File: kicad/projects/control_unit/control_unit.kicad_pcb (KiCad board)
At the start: 2 copper layers, 177.8 x 76.2 mm, 20 parts, among them J1 Conn_01x11_Male, J2 Conn_01x04_Female, J3 Conn_01x08_Female, J4 Conn_01x34_Male, J5 Conn_01x16_Female, J6 Conn_01x16_Female, J7 Conn_01x08_Female, J8 Conn_01x01_Female, U1 28C256, U2 28C256, U3 28C256, U4 28C256, U5 74HCT377, U6 74HCT161, U7 74HCT173, U8 74HCT138, U9 74HCT04

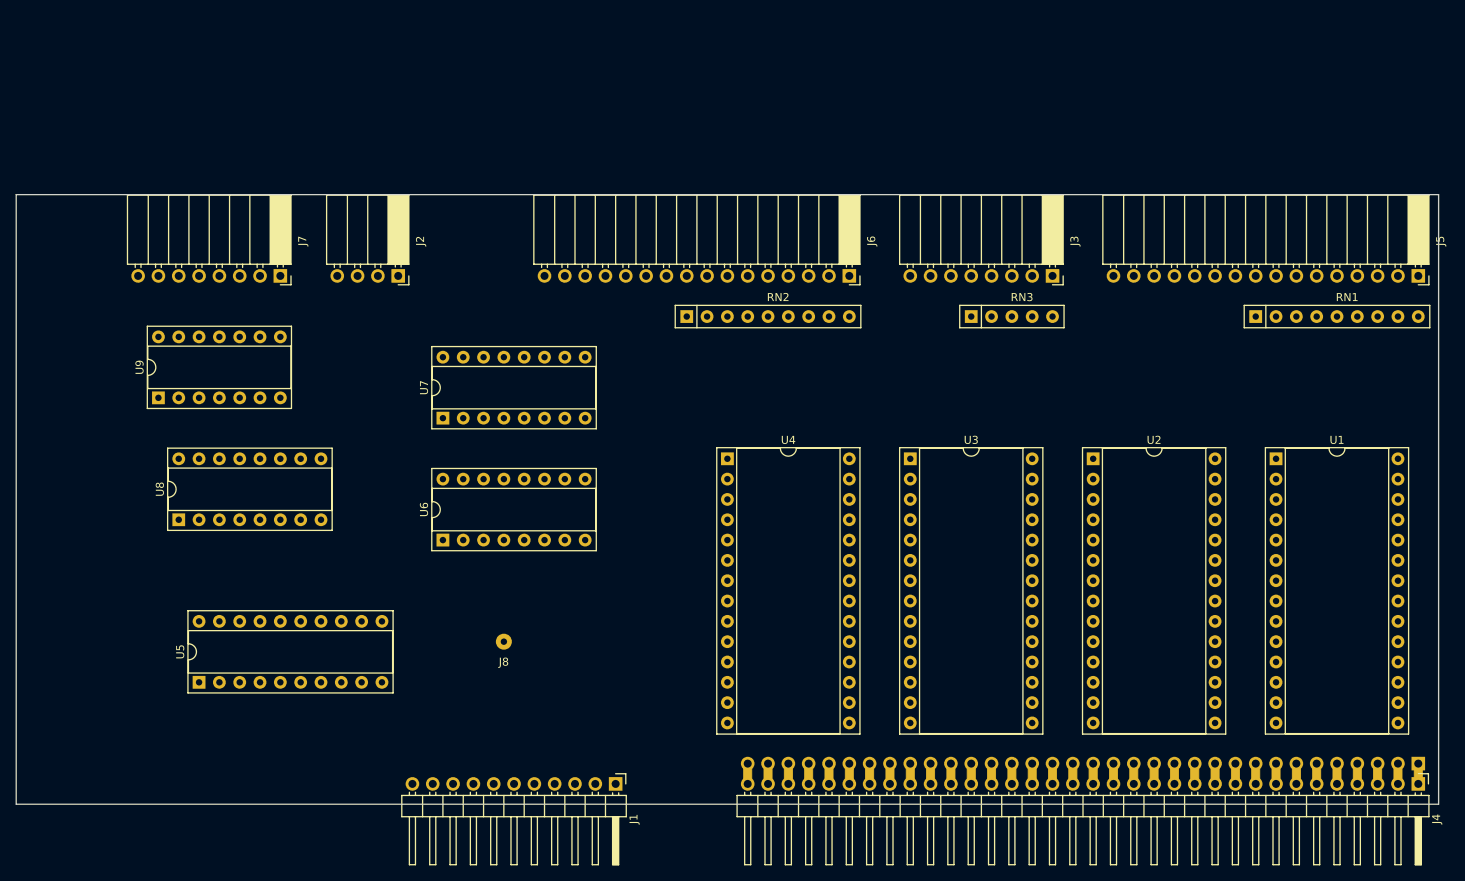
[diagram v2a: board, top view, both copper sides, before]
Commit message: Start pcblayout on cu. Fix small path messiness on register.
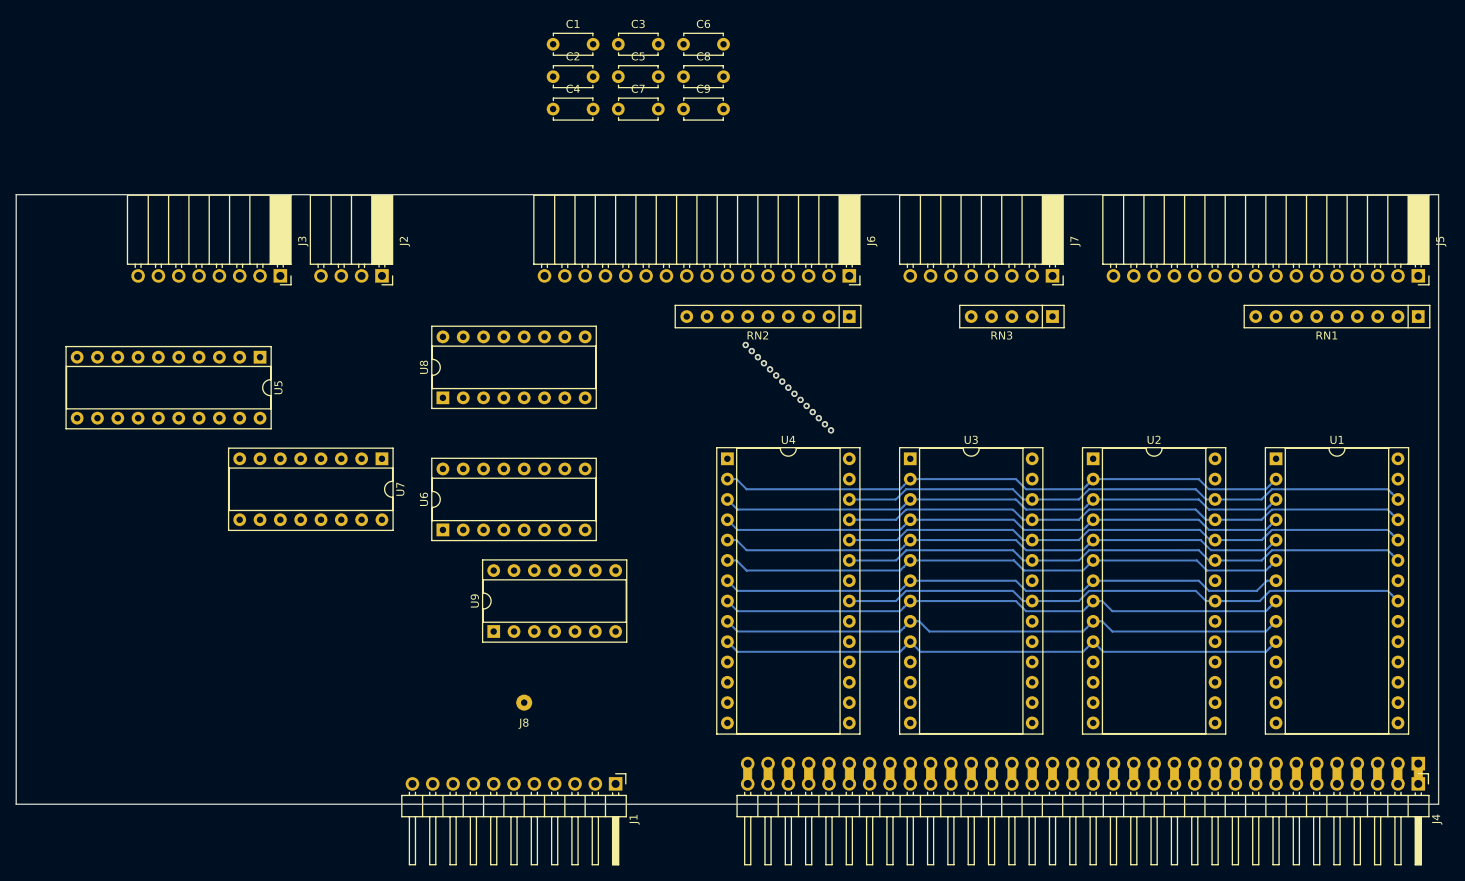
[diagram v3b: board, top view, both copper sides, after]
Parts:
- added C1: 100nF, Capacitor_THT:C_Disc_D4.7mm_W2.5mm_P5.00mm, F.Cu at (112.8, 24.4)
- added C2: 100nF, Capacitor_THT:C_Disc_D4.7mm_W2.5mm_P5.00mm, F.Cu at (112.8, 28.4)
- added C3: 100nF, Capacitor_THT:C_Disc_D4.7mm_W2.5mm_P5.00mm, F.Cu at (121.0, 24.4)
- added C4: 100nF, Capacitor_THT:C_Disc_D4.7mm_W2.5mm_P5.00mm, F.Cu at (112.8, 32.5)
- added C5: 100nF, Capacitor_THT:C_Disc_D4.7mm_W2.5mm_P5.00mm, F.Cu at (121.0, 28.4)
- added C6: 100nF, Capacitor_THT:C_Disc_D4.7mm_W2.5mm_P5.00mm, F.Cu at (129.1, 24.4)
- added C7: 100nF, Capacitor_THT:C_Disc_D4.7mm_W2.5mm_P5.00mm, F.Cu at (121.0, 32.5)
- added C8: 100nF, Capacitor_THT:C_Disc_D4.7mm_W2.5mm_P5.00mm, F.Cu at (129.1, 28.4)
- added C9: 100nF, Capacitor_THT:C_Disc_D4.7mm_W2.5mm_P5.00mm, F.Cu at (129.1, 32.5)
- J1: value Conn_01x11_Male -> BUS
- J2: value Conn_01x04_Female -> FLAGS
- J3: value Conn_01x08_Female -> INSTRUCTION
- J4: value Conn_01x34_Male -> BACKPLANE
- J5: value Conn_01x16_Female -> MIR INST LEDS
- J6: value Conn_01x16_Female -> STEP LEDS
- J7: value Conn_01x08_Female -> MIR FLAG LEDS
- J8: value Conn_01x01_Female -> STEP RESET
- RN1: value R_Network08_US -> MIR INST RESISTORS
- RN2: value R_Network08_US -> STEP RESISTORS
- RN3: value R_Network04_US -> MIR FLAG RESISTORS
- moved J3 96.5 mm to (78.7, 53.3)
- moved J7 96.5 mm to (175.3, 53.3)
- moved U9 51.1 mm to (105.4, 97.8)
- moved U5 41.3 mm to (76.2, 63.5), turned to 270 degrees
- moved U8 36.4 mm to (99.1, 68.6)
- moved RN2 20.3 mm to (149.9, 58.4), turned to 180 degrees
- moved RN1 20.3 mm to (221.0, 58.4), turned to 180 degrees
- moved RN3 10.2 mm to (175.3, 58.4), turned to 180 degrees
- moved U7 9.16 mm to (91.4, 76.2), turned to 270 degrees
- moved J8 8.03 mm to (109.2, 106.7)
- moved J2 2.03 mm to (91.4, 53.3)
- moved U6 1.27 mm to (99.1, 85.1)
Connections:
- J1 pad 10: Net-(J1-Pad10) -> GND
- J1 pad 9: Net-(J1-Pad9) -> VCC
- RN1 pad 1: Net-(RN1-Pad1) -> GND
- RN2 pad 1: Net-(RN2-Pad1) -> VCC
- RN3 pad 1: Net-(RN3-Pad1) -> GND
- U1 pad 20: Net-(U1-Pad20) -> GND
- U1 pad 22: Net-(U1-Pad22) -> GND
- U1 pad 27: Net-(U1-Pad27) -> VCC
- U1 pad 28: Net-(U1-Pad28) -> VCC
- U2 pad 27: Net-(U2-Pad27) -> VCC
- U2 pad 28: Net-(U2-Pad28) -> VCC
- U3 pad 27: Net-(U3-Pad27) -> VCC
- U3 pad 28: Net-(U3-Pad28) -> VCC
- U4 pad 27: Net-(U4-Pad27) -> VCC
- U4 pad 28: Net-(U4-Pad28) -> VCC
- U5 pad 20: Net-(U5-Pad20) -> VCC
- U6 pad 16: Net-(U6-Pad16) -> VCC
- U6 pad 8: Net-(U6-Pad8) -> GND
- U7 pad 16: Net-(U7-Pad16) -> VCC
- U7 pad 8: Net-(U7-Pad8) -> GND
- U8 pad 16: Net-(U8-Pad16) -> VCC
- U8 pad 4: Net-(U8-Pad4) -> GND
- U8 pad 5: Net-(U8-Pad5) -> GND
- U8 pad 6: Net-(U8-Pad6) -> VCC
- U8 pad 8: Net-(U8-Pad8) -> GND
- U9 pad 11: Net-(U9-Pad11) -> GND
- U9 pad 13: Net-(U9-Pad13) -> GND
- U9 pad 14: Net-(U9-Pad14) -> VCC
- U9 pad 5: Net-(U9-Pad5) -> GND
- U9 pad 7: Net-(U9-Pad7) -> GND
- U9 pad 9: Net-(U9-Pad9) -> GND
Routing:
- net /MIR_INST_3: track 0.00 -> 71.7 mm
- net /MIR_INST_5: track 0.00 -> 71.7 mm
- net /MIR_FLAG_E: track 0.00 -> 71.7 mm
- net /MC_STEP_1: track 0.00 -> 71.7 mm
- net /MIR_INST_4: track 0.00 -> 71.7 mm
- net /MIR_INST_6: track 0.00 -> 71.7 mm
- net /MIR_INST_1: track 0.00 -> 71.7 mm
- net /MIR_FLAG_Z: track 0.00 -> 71.7 mm
- net /MIR_FLAG_N: track 0.00 -> 71.7 mm
- net /MIR_FLAG_C: track 0.00 -> 71.7 mm
- net /MC_STEP_2: track 0.00 -> 71.7 mm
- net /MIR_INST_2: track 0.00 -> 71.7 mm
- net /MIR_INST_0: track 0.00 -> 71.7 mm
- net /MC_STEP_0: track 0.00 -> 71.7 mm
- net (no net): vias 0 -> 15
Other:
- net class Default: clearance 0.2 -> 0.127; trace_width 0.25 -> 0.254
- rule trace_clearance: 0.2 -> 0.127

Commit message: Layout setp counter and flag chips on control unit PCB.
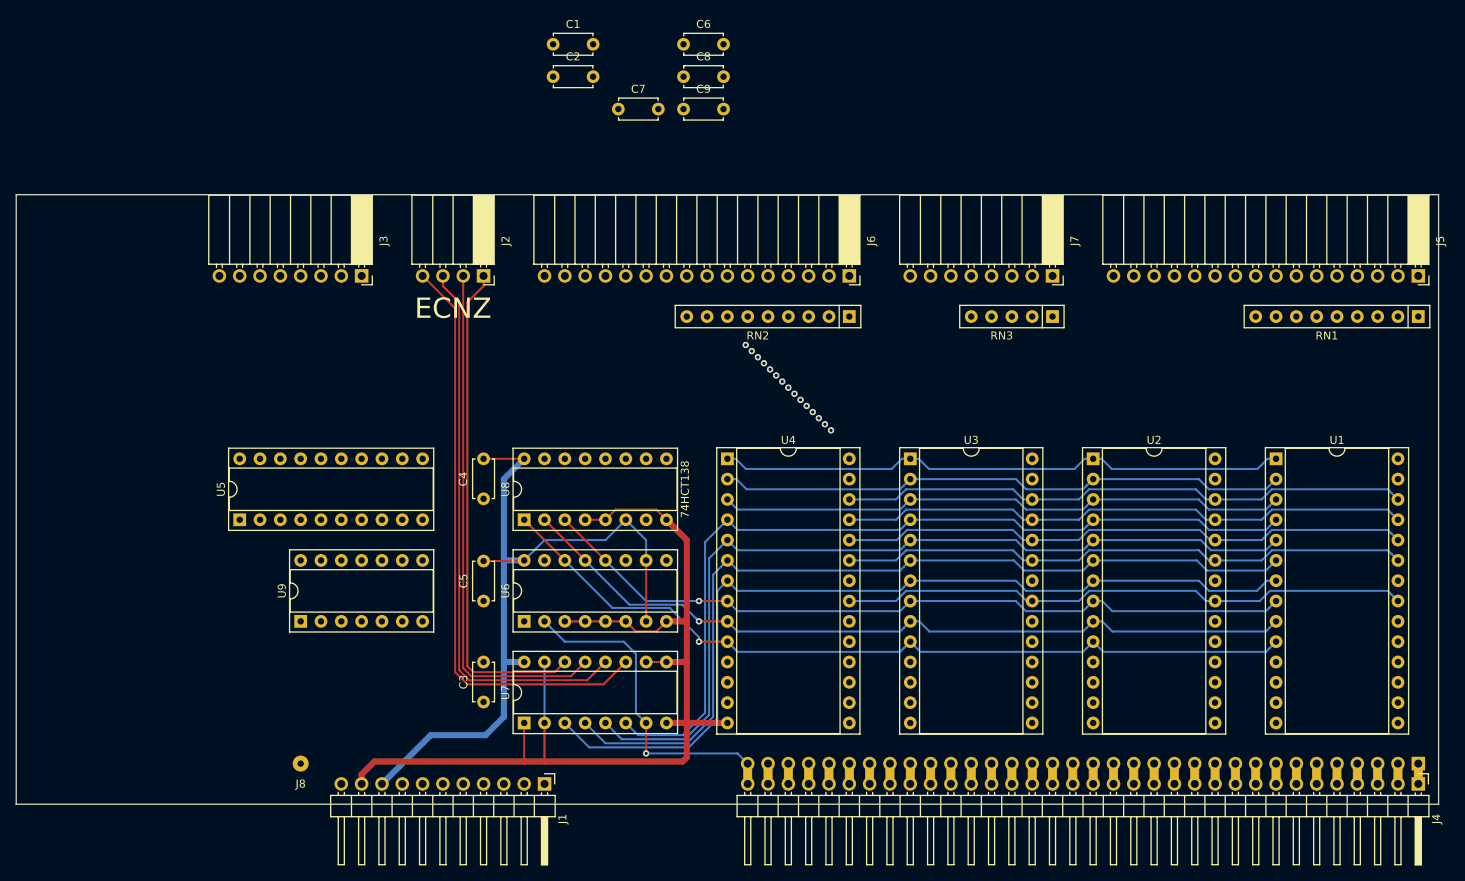
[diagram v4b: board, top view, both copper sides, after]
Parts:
- moved C3 83.9 mm to (104.1, 106.6), turned to 90 degrees
- moved C5 67.7 mm to (104.1, 94.0), turned to 90 degrees
- moved C4 44.6 mm to (104.1, 76.2), turned to 270 degrees
- moved U7 37.5 mm to (109.2, 109.2), turned to 90 degrees
- moved J8 29.0 mm to (81.3, 114.3)
- moved U9 24.2 mm to (81.3, 96.5)
- moved U5 20.5 mm to (73.7, 83.8), turned to 90 degrees
- moved U8 18.3 mm to (109.2, 83.8)
- moved U6 15.3 mm to (109.2, 96.5)
- moved J2 12.7 mm to (104.1, 53.3)
- moved J3 10.2 mm to (88.9, 53.3)
- moved J1 8.89 mm to (111.8, 116.8)
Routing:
- net GND: track 0.00 -> 131.0 mm
- net VCC: track 0.00 -> 95.9 mm
- net Net-(J2-Pad4): track 0.00 -> 74.3 mm
- net /MIR_INST_7: track 0.00 -> 71.7 mm
- net Net-(J2-Pad3): track 0.00 -> 69.9 mm
- net Net-(J2-Pad2): track 0.00 -> 65.4 mm
- net Net-(J2-Pad1): track 0.00 -> 62.6 mm
- net /MIR_FLAG_Z: track 71.7 -> 111.3 mm
- net /CONTROL_CLOCK: track 0.00 -> 39.3 mm, vias 0 -> 1
- net /MIR_FLAG_N: track 71.7 -> 110.5 mm
- net /MIR_FLAG_C: track 71.7 -> 109.6 mm
- net /MIR_FLAG_E: track 71.7 -> 108.7 mm
- net /MC_STEP_0: track 71.7 -> 103.8 mm, vias 0 -> 1
- net /MC_STEP_1: track 71.7 -> 99.9 mm, vias 0 -> 1
- net /MC_STEP_2: track 71.7 -> 96.3 mm, vias 0 -> 1
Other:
- net class Default: clearance 0.127 -> 0.1524
- rule trace_clearance: 0.127 -> 0.1524
- board text added: "ECNZ"

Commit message: Tiny bit of work - mostly re-familiarising myself with KiCad.
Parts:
- added J9: MASTER RESET, Connector_PinSocket_2.54mm:PinSocket_1x01_P2.54mm_Horizontal, F.Cu at (63.5, 53.3)
- moved C9 77.4 mm to (76.2, 88.9), turned to 270 degrees
- moved C1 72.1 mm to (68.6, 81.3), turned to 90 degrees
- moved C7 13.8 mm to (107.4, 35.1)
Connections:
- U9 pad 1: /MASTER_RESET -> Net-(J9-Pad1)
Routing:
- net GND: track 131.0 -> 175.6 mm
- net Net-(U6-Pad9): track 0.00 -> 41.3 mm, vias 0 -> 2
- net Net-(U6-Pad1): track 0.00 -> 26.7 mm, vias 0 -> 1
- net Net-(J8-Pad1): track 0.00 -> 19.9 mm

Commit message: More work on kicad control unit pcb
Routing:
- net /MIR_INST_0: track 71.7 -> 231.6 mm, vias 0 -> 2
- net /MIR_INST_1: track 71.7 -> 223.2 mm, vias 0 -> 2
- net /MIR_INST_2: track 71.7 -> 220.4 mm, vias 0 -> 2
- net /MIR_INST_7: track 71.7 -> 217.5 mm, vias 0 -> 3
- net /MIR_INST_6: track 71.7 -> 213.0 mm, vias 0 -> 2
- net /MIR_INST_5: track 71.7 -> 211.0 mm, vias 0 -> 2
- net /MIR_INST_3: track 71.7 -> 210.7 mm, vias 0 -> 2
- net /MIR_INST_4: track 71.7 -> 204.3 mm, vias 0 -> 2
- net Net-(J6-Pad1): track 0.00 -> 53.7 mm, vias 0 -> 1
- net Net-(J6-Pad3): track 0.00 -> 52.5 mm, vias 0 -> 2
- net Net-(J6-Pad5): track 0.00 -> 45.8 mm, vias 0 -> 2
- net Net-(J6-Pad7): track 0.00 -> 38.5 mm, vias 0 -> 2
- net Net-(J6-Pad15): track 0.00 -> 34.7 mm
- net Net-(J6-Pad9): track 0.00 -> 32.7 mm
- net Net-(J6-Pad13): track 0.00 -> 26.0 mm
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
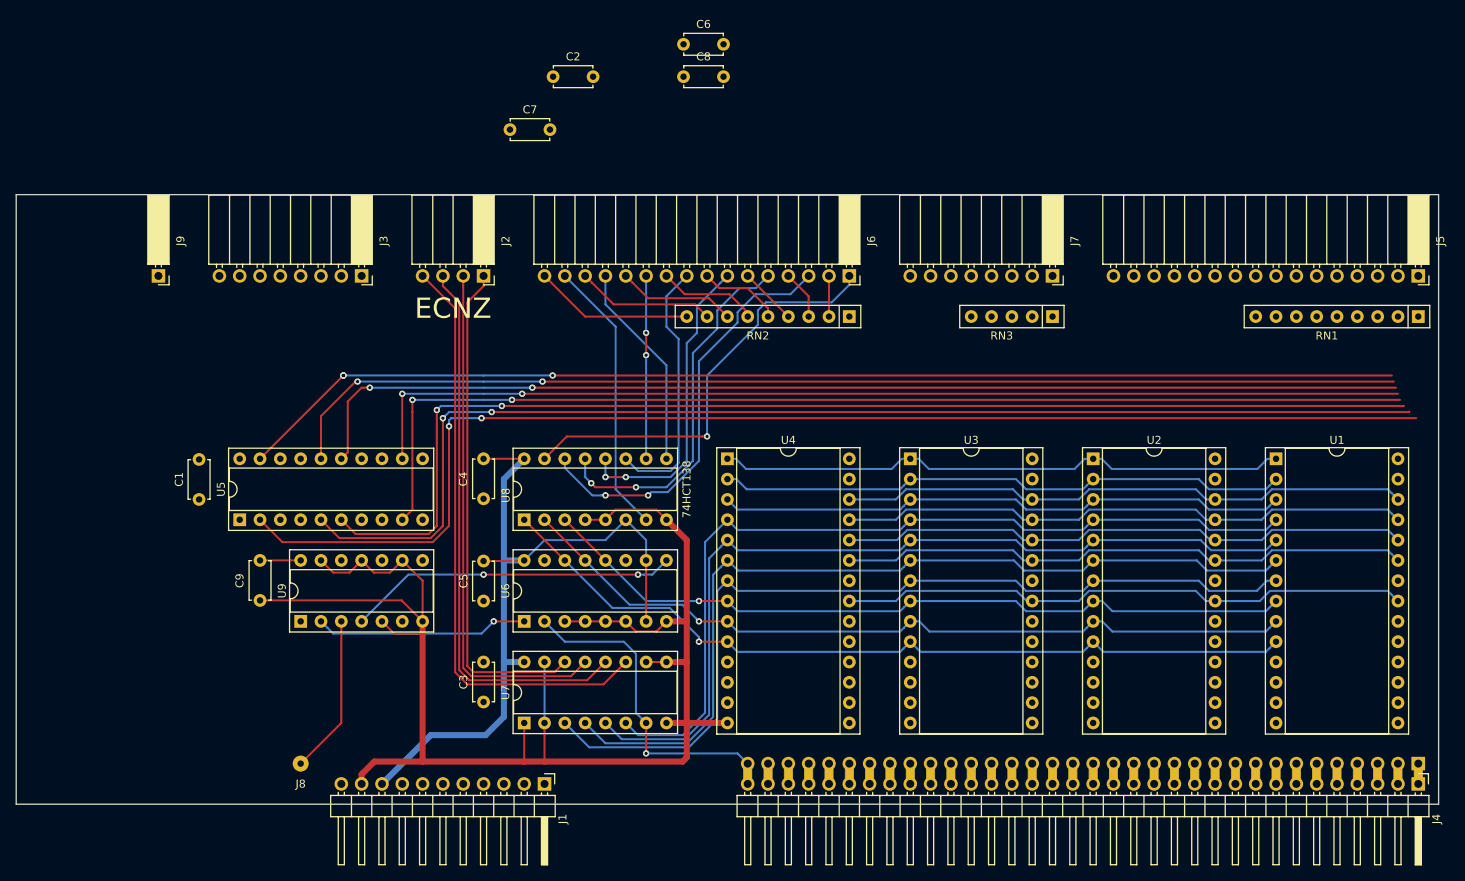
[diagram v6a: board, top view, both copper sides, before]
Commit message: Add rom power rails and connect instruction LEDs
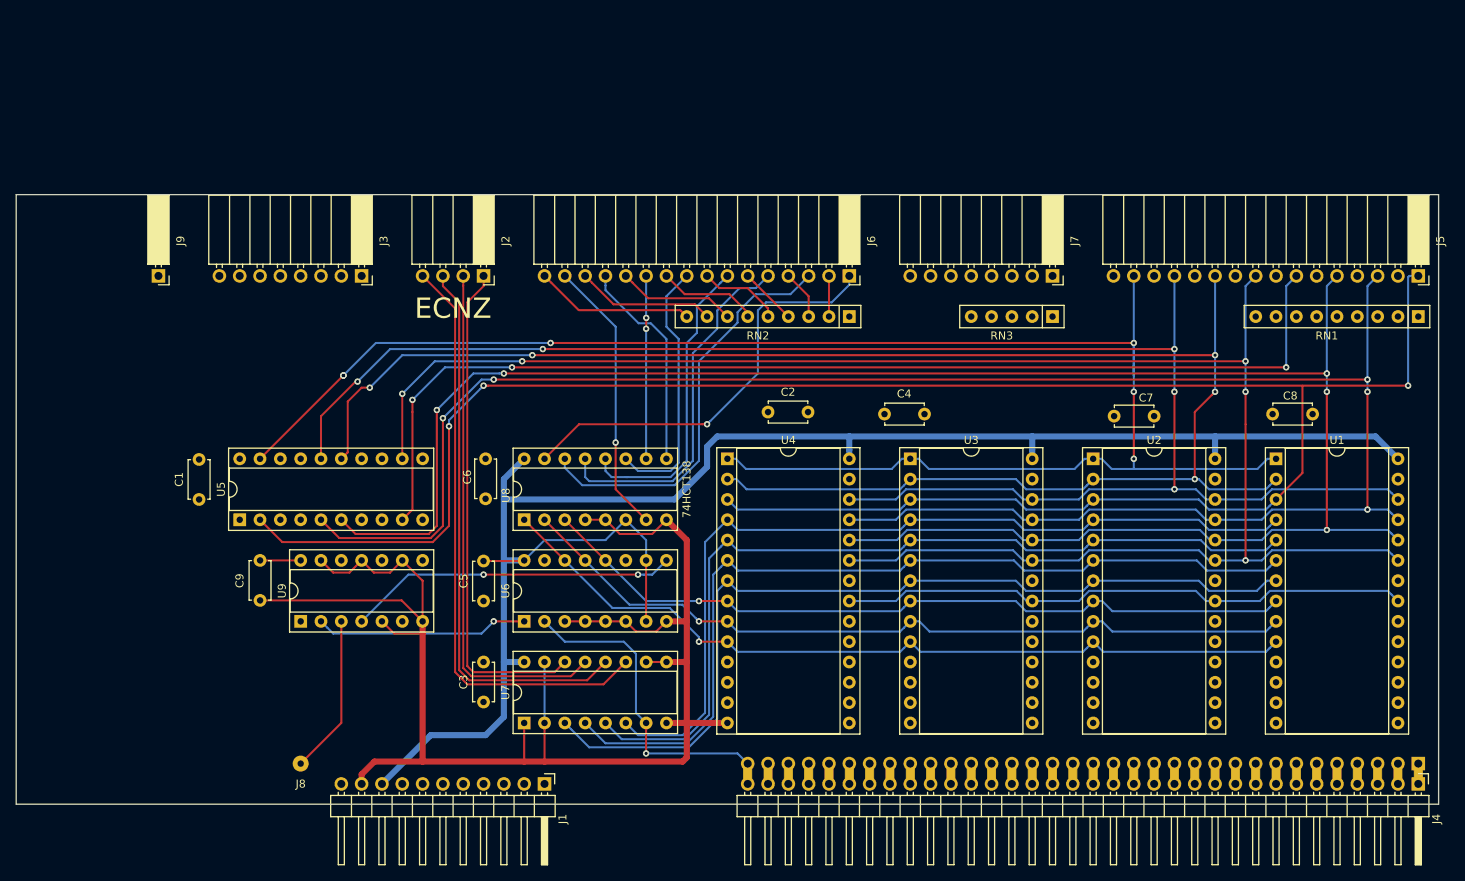
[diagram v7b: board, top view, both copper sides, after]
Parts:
- moved C8 89.2 mm to (207.8, 70.6), turned to 180 degrees
- moved C7 88.1 mm to (188.0, 70.9), turned to 180 degrees
- moved C6 57.4 mm to (104.4, 76.2), turned to 270 degrees
- moved C4 55.4 mm to (159.3, 70.6), turned to 180 degrees
- moved C2 49.8 mm to (139.7, 70.4)
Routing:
- net VCC: track 100.9 -> 221.9 mm
- net /MIR_INST_0: track 231.6 -> 262.7 mm, vias 2 -> 3
- net /MIR_INST_1: track 223.2 -> 249.3 mm, vias 2 -> 5
- net /MIR_INST_2: track 220.4 -> 244.7 mm, vias 2 -> 5
- net /MIR_INST_4: track 204.3 -> 223.0 mm, vias 2 -> 5
- net /MIR_INST_5: track 211.0 -> 216.5 mm, vias 2 -> 5
- net /MIR_INST_7: track 217.5 -> 216.4 mm, vias 3 -> 6
- net Net-(J6-Pad3): track 52.5 -> 51.4 mm, vias 2 -> 0
- net /MIR_INST_6: track 213.0 -> 213.9 mm, vias 2 -> 5
- net Net-(J6-Pad1): track 53.7 -> 52.8 mm
- net Net-(J6-Pad13): track 26.0 -> 26.9 mm
- net Net-(J6-Pad5): track 45.8 -> 45.2 mm, vias 2 -> 0
- net /MIR_INST_3: track 210.7 -> 210.1 mm, vias 2 -> 3
- net Net-(J6-Pad7): track 38.5 -> 38.3 mm, vias 2 -> 0
- net Net-(J6-Pad15): vias 0 -> 1
